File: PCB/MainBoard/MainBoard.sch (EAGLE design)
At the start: 79 parts, among them Q1 CSM-7X-DU, U1 STMICROELECTRONICS_STM32F446R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, U2 TI_NATIONAL_SEMICONDUCTOR_LM1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, U3 STMICROELECTRONICS_L78M05CDT-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

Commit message: Main board updates
-change mcu(STM32H753)
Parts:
- removed C20: 100nF, rcl:C-EUC0805
- removed C34: 10uF, rcl:C-EUC0805
- removed Q1: CSM-7X-DU, crystal:CSM-7X-DU
- removed U2: TI_NATIONAL_SEMICONDUCTOR_LM1117DT-3.3TI_NATIONAL_SEMICONDU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, TI National Semiconductor - LM1117DT-3.3:TI_NATIONAL_SEMICONDUCTOR_LM1117DT-3.3TI_NATIONAL_SEMICONDUCTOR_LM1117DT-3.3_0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
- removed U3: STMICROELECTRONICS_L78M05CDT-TRSTMICROELECTRONICS_L78M05CDT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, STMicroelectronics - L78M05CDT-TR:STMICROELECTRONICS_L78M05CDT-TRSTMICROELECTRONICS_L78M05CDT-TR_0_2
- added C40, C41, C42: 100nF, rcl:C-EUC0805
- added C43, C44, C45: 10uF, rcl:C-EUC0805
- added C46, C47: 22p, rcl:C-EUC0805
- added IC1: LD1085D2T33R, SamacSys_Parts:LD1085D2T33R
- added Q2: CSM-7X-DU, crystal:CSM-7X-DU
- added U4: STM32H753VIT6, STM32H753VIT6:STM32H753VIT6
- added U5: LM1084IS-5.0/NOPB, LM1084IS-5.0_NOPB:LM1084IS-5.0/NOPB
- C2, C3, C6, C7: device rcl:CPOL-EUC -> rcl:C-EUC0805
- C24: value 4,7uF(ceramic) -> 100nF
- C26: value 22p -> 2.2uf(ceramic)
- C27: value 22p -> 100uF
- U1: value STMICROELECTRONICS_STM32F446RET6STMICROELECTRONICS_STM32F446RET6_0_1 -> LM1084IS-5.0/NOPB; device STMicroelectronics - STM32F446RET6:STMICROELECTRONICS_STM32F446RET6STMICROELECTRONICS_STM32F446RET6_0_1 -> LM1084IS-5.0_NOPB:LM1084IS-5.0/NOPB
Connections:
- removed net BUTTON_1: U1B.PB15
- removed net BUTTON_2: U1B.PB14
- removed net BUTTON_3: U1B.PB13
- new net N$10: C47.1, Q2.2, U4G$1.PH0/OSC_IN
- new net N$11: C46.1, Q2.1, U4G$1.PH1/OSC_OUT
- new net N$12: U4G$2.PB10/QUADSPI_BK1_NCS
- new net N$13: U4G$2.PC9/QUADSPI_BK1_IO0
- new net N$14: U4G$2.PD11/QUADSPI_BK1_IO0
- new net N$15: U4G$2.PC10/QUADSPI_BK1_IO1
- new net N$16: U4G$2.PE2/QUADSPI_BK1_IO2
- new net N$19: U4G$2.PC11/QUADSPI_BK2_NCS
- new net N$20: U4G$2.PE7/QUADSPI_BK2_IO0
- new net N$22: U4G$2.PE9/QUADSPI_BK2_IO2
- new net N$23: U4G$2.PE10/QUADSPI_BK2_IO3
- new net N$25: U4G$2.PA5/SPI1_SCK/I2S1_CK
- new net N$26: U4G$2.PA6/SPI1_MISO/I2S1_SD
- new net N$27: U4G$2.PA7/SPI1_MOSI/I2S1_SDO
- new net N$28: U4G$2.PA15/SPI1_NSS/I2S1_WS
- new net N$29: U4G$2.PB3/SPI1_SCK/I2S1_CK
- new net N$30: U4G$2.PB4/SPI1_MISO/I2S1_SD
- new net N$31: U4G$2.PB5/SPI1_MOSI/I2S1_SDO
- new net N$32: U4G$2.PD7/SPI1_MOSI/I2S1_SDO
- new net N$33: U4G$3.PA0
- new net N$34: U4G$3.PA1
- new net N$35: U4G$3.PA2
- new net N$36: U4G$3.PA3
- new net N$37: U4G$3.PA8
- new net N$38: U4G$3.PB0
- new net N$39: U4G$3.PB1
- new net N$40: U4G$3.PB7
- new net N$41: U4G$3.PB8
- new net N$42: U4G$3.PB9
- new net N$43: U4G$3.PC0
- new net N$44: U4G$3.PC1
- new net N$47: U4G$3.PC4
- new net N$48: U4G$3.PC5
- new net N$49: U4G$3.PD0
- new net N$50: U4G$3.PD1
- new net N$51: U4G$3.PD2
- new net N$53: U4G$3.PD4
- new net N$54: U4G$3.PD5
- new net N$55: U4G$3.PE0
- new net N$56: U4G$3.PE1
- new net N$57: U4G$3.PE3
- new net N$58: U4G$3.PE4
- new net N$59: U4G$3.PE5
- new net N$60: U4G$3.PE6
- new net N$61: U4G$3.PE15
- new net N$62: U4G$3.PE14
- new net N$63: U4G$3.PE13
- new net N$64: U4G$3.PE12
- new net N$65: U4G$3.PE11
- new net N$66: U4G$3.PD15
- new net N$67: U4G$3.PD14
- new net N$68: U4G$3.PD10
- new net N$69: U4G$3.PD9
- new net N$70: U4G$3.PD8
- new net N$71: U4G$3.PD6
- new net N$72: U4G$3.PC13
- new net N$73: U4G$3.PC12
- new net N$74: U4G$3.PC8
- new net N$75: U4G$3.PC7
- new net N$76: U4G$3.PC6
- new net N$77: U4G$3.PB15
- new net N$78: U4G$3.PB14
- new net N$79: U4G$3.PB13
- new net N$80: U4G$3.PB12
- new net N$81: U4G$3.PB11
- new net N$82: U4G$3.PA12
- new net N$83: U4G$3.PA9
- new net N$84: U4G$3.PA10
- new net N$85: U4G$3.PA11
- new net N$86: U4G$1.PA13/JTMS-SWDIO
- new net N$87: U4G$1.PA14/JTCK-SWCLK
- net +3V3: now also C40.2, C41.2, C42.2, C43.2, C44.2, C45.2, U4G$1.VBAT, U4G$1.VDD, U4G$1.VDDA; no longer C20.2, C34.2, U1A.1_VDD, U1A.2_VDD, U1A.3_VDD, U1A.4_VDD, U1A.VBAT
- net +5V: now also C3.1, U1.OUTPUT; no longer C3.+, U3.OUT
- net 3V3: now also C7.1, IC1.OUTPUT; no longer C7.+, U2.OUT
- net A3V3: now also U4G$1.VREF+; no longer U1A.VDDA
- net BAT_ADC: no longer U1B.PA7
- net DIR_L1: no longer U1B.PC0
- net DIR_L2: no longer U1B.PC1
- net DIR_P1: no longer U1B.PC2
- net DIR_P2: no longer U1B.PC3
- net ENK_LP_A: no longer U1B.PA8
- net ENK_LP_B: no longer U1B.PA9
- net ENK_LT_A: no longer U1B.PA15
- net ENK_LT_B: no longer U1B.PB3
- net ENK_PP_A: no longer U1B.PC6
- net ENK_PP_B: no longer U1B.PC7
- net ENK_PT_A: no longer U1B.PB6
- net ENK_PT_B: no longer U1B.PB7
- net GND: now also C2.2, C24.2, C27.2, C3.2, C40.1, C41.1, C42.1, C43.1, C44.1, C45.1, C46.2, C47.2, C6.2, C7.2, IC1.GND, R1.1, U1.ADJ/GND, U4G$1.VSS, U4G$1.VSSA, U5.ADJ/GND; no longer C2.-, C20.1, C24.1, C27.1, C3.-, C34.1, C6.-, C7.-, R1.2, U1A.1_VSS, U1A.2_VSS, U1A.3_VSS, U1A.4_VSS, U1A.VSSA, U2.GND, U3.GND
- net KTIR_1: no longer U1B.PA4
- net KTIR_2: no longer U1B.PA5
- net KTIR_3: no longer U1B.PA6
- net LED_1: no longer U1B.PA12
- net LED_2: no longer U1B.PA11
- net LED_3: no longer U1B.PA10
- net N$1: now also C25.2, R2.1, U4G$1.!RST; no longer C26.2, Q1.1, U1B.PH1-OSC_OUT
- net N$17: now also U4G$2.PD12/QUADSPI_BK1_IO1; no longer U1B.PC8
- net N$18: now also U4G$2.PD13/QUADSPI_BK1_IO3; no longer U1B.PC9
- net N$2: now also U4G$2.PB2/QUADSPI_CLK; no longer C24.2, U1A.VCAP_1
- net N$21: now also U4G$2.PE8/QUADSPI_BK2_IO1; no longer U1B.PC12
- net N$24: now also U4G$2.PA4/SPI1_NSS/I2S1_WS; no longer U1B.PC15-OSC32_OUT
- net N$3: now also R1.2, U4G$1.BOOT0; no longer R1.1, U1B.BOOT0
- net N$4: now also C26.2, U4G$1.VCAP; no longer C27.2, Q1.2, U1B.PH0-OSC_IN
- net N$45: now also U4G$3.PC2_C; no longer U1B.PB4
- net N$46: now also U4G$3.PC3_C; no longer U1B.PB5
- net N$52: now also U4G$3.PD3; no longer U1B.PB12
- net N$8: now also U4G$2.PB6/QUADSPI_BK1_NCS; no longer U1B.PD2
- net NRST: no longer C25.2, R2.1, U1B.!RST!
- net PWM_LP: no longer U1B.PA0
- net PWM_LT: no longer U1B.PA1
- net PWM_PP: no longer U1B.PA2
- net PWM_PT: no longer U1B.PA3
- net RX: no longer U1B.PC11
- net SCL: no longer U1B.PB8
- net SDA: no longer U1B.PB9
- net SHARP_1: no longer U1B.PC4
- net SHARP_2: no longer U1B.PC5
- net SHARP_3: no longer U1B.PB0
- net SHARP_4: no longer U1B.PB1
- net SHARP_5: no longer U1B.PB2
- net SHARP_6: no longer U1B.PB10
- net SWCLK: no longer U1B.PA14
- net SWDIO: no longer U1B.PA13
- net S_KILL: no longer U1B.PC14-OSC32_IN
- net S_START: no longer U1B.PC13
- net TX: no longer U1B.PC10
- net V_BAT: now also C2.1, C24.1, C27.1, C6.1, IC1.INPUT, U1.INPUT, U5.INPUT, U5.OUTPUT; no longer C2.+, C6.+, U2.IN, U3.IN
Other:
- moved on the sheet: C24, C25, C26, C27, C38, C39, C4, C5, C8, R1, R2, R9

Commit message: Update eagle files
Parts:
- removed C1, C4: 100nF, rcl:C-EUC0805
- removed C2, C3: 100uF, rcl:C-EUC0805
- removed U1: LM1084IS-5.0/NOPB, LM1084IS-5.0_NOPB:LM1084IS-5.0/NOPB
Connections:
- new net N$88: C24.2, C27.2, U5.ADJ/GND
- net +5V: now also C5.1, C6.1, IC1.INPUT, U5.OUTPUT; no longer C3.1, C4.1, U1.OUTPUT
- net GND: no longer C1.2, C2.2, C24.2, C27.2, C3.2, C4.2, U1.ADJ/GND, U5.ADJ/GND
- net V_BAT: no longer C1.1, C2.1, C5.1, C6.1, IC1.INPUT, U1.INPUT, U5.OUTPUT
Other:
- moved on the sheet: C24, C27, C5, C6, U5

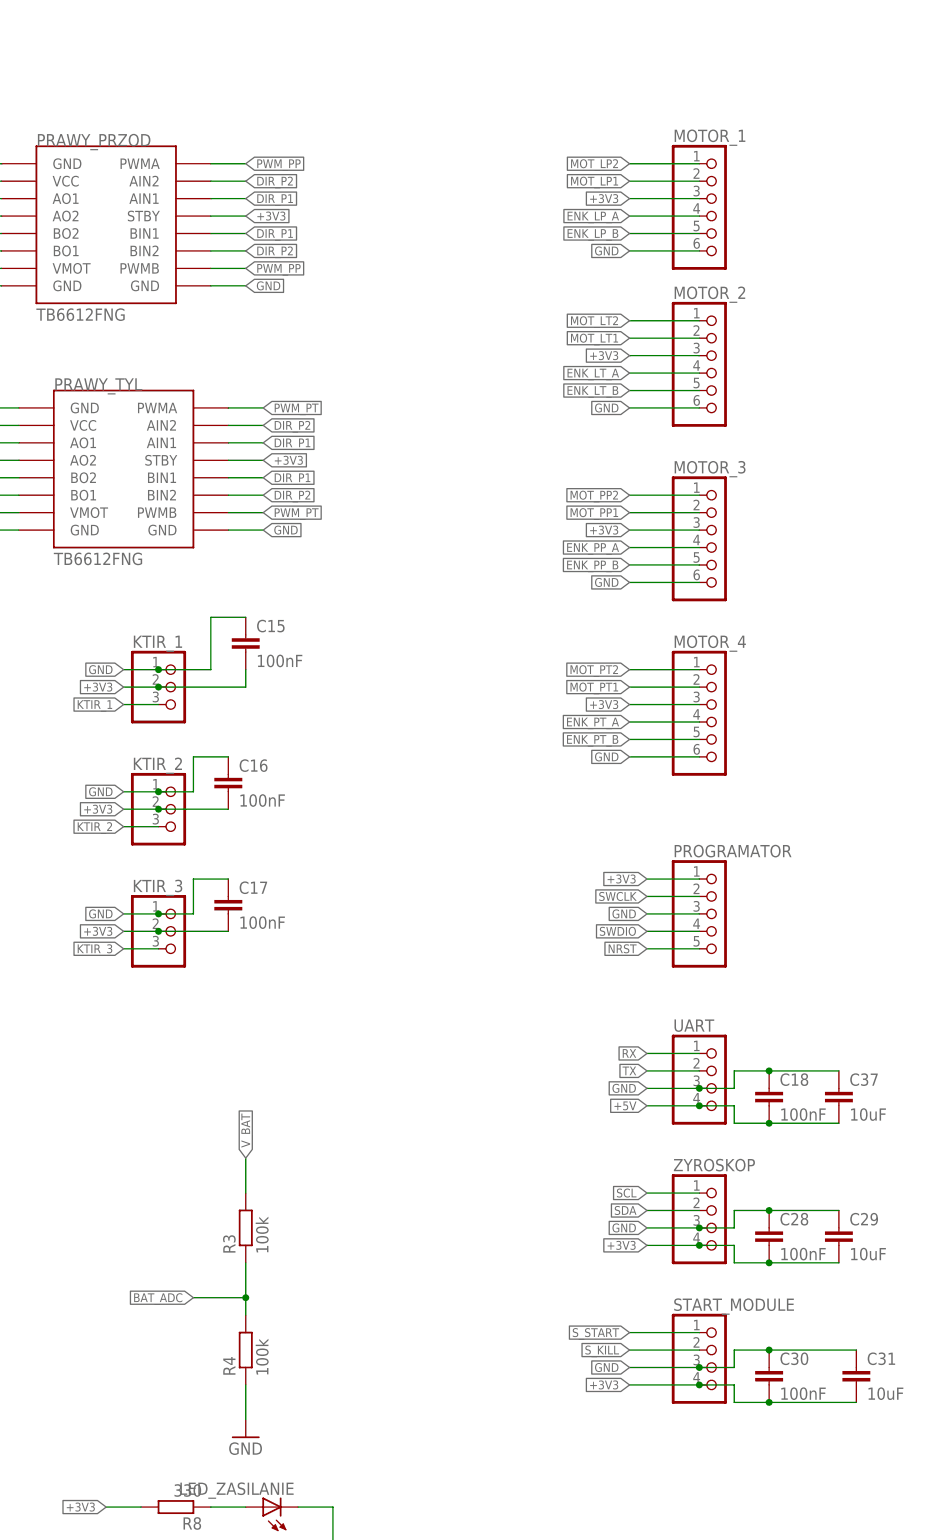
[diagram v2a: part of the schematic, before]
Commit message: PCB update
-place elements on the board
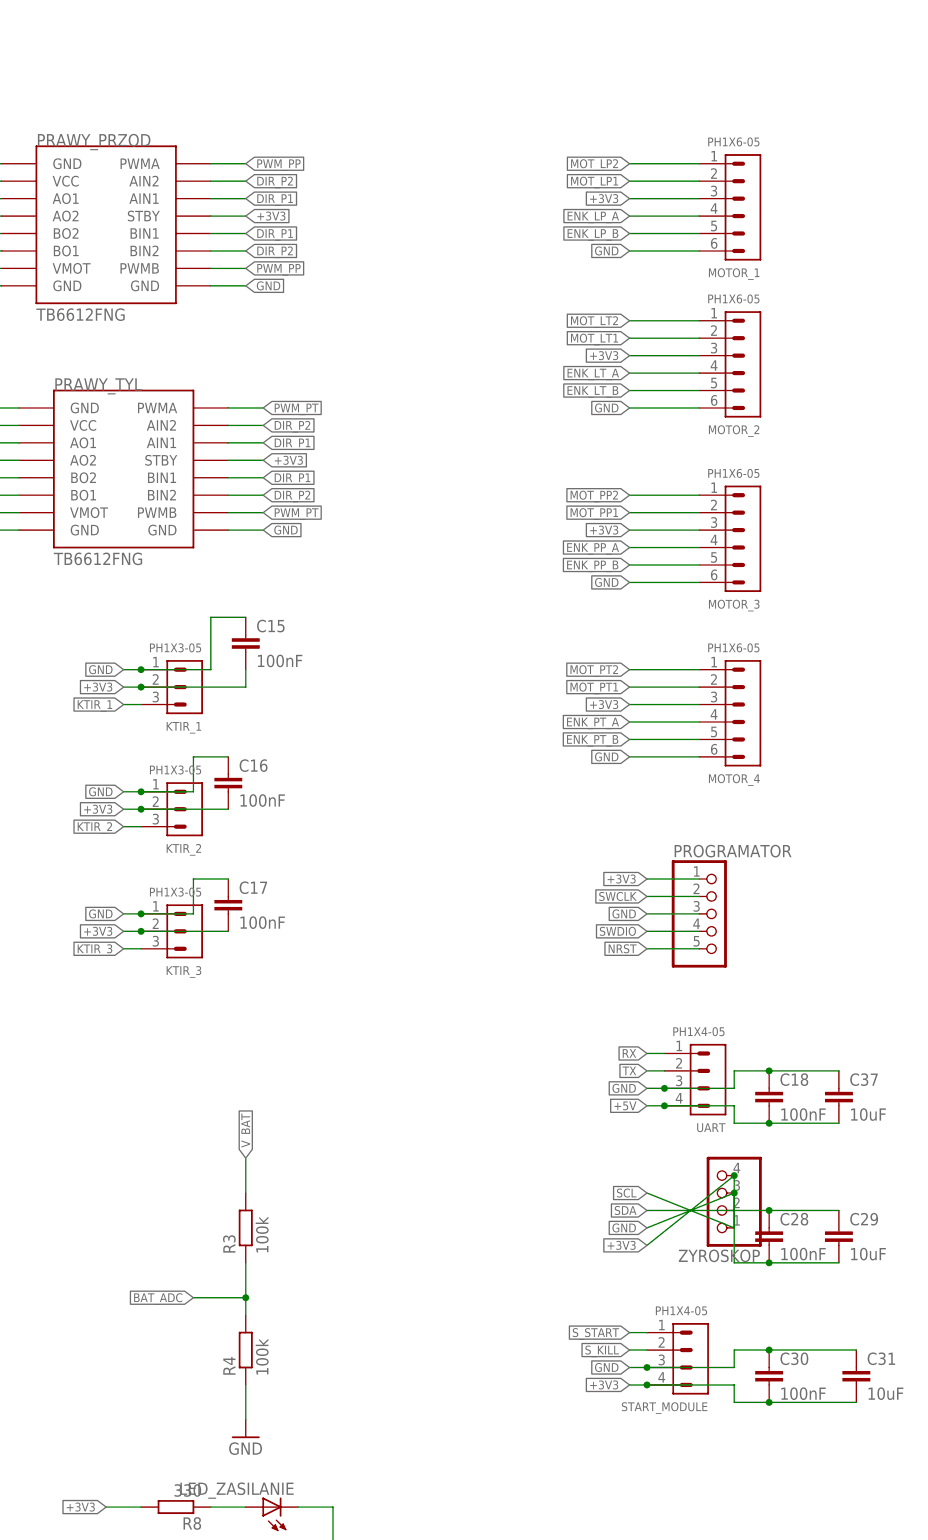
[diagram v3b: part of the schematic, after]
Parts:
- KTIR_1, KTIR_2, KTIR_3: value (none) -> PH1X3-05; device pinhead:PINHD-1X3 -> pinhrad:PH1X3-05
- MOTOR_1, MOTOR_2, MOTOR_3, MOTOR_4: value (none) -> PH1X6-05; device pinhead:PINHD-1X6 -> pinhrad:PH1X6-05
- START_MODULE, UART: value (none) -> PH1X4-05; device pinhead:PINHD-1X4 -> pinhrad:PH1X4-05
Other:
- moved on the sheet: ZYROSKOP

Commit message: Update pcb files
- edit positions on the board
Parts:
- added R13: 100R, rcl:R-EU_M0805
- added R14, R15: 47R, rcl:R-EU_M0805
- PROGRAMATOR: value (none) -> FTSH-107-01-F-DV-K; device pinhead:PINHD-1X5 -> FTSH-107-01-F-DV-K:FTSH-107-01-F-DV-K
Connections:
- net N$30 renamed JRST
- removed net N$18: U4G$2.PD13/QUADSPI_BK1_IO3
- removed net N$22: U4G$2.PE9/QUADSPI_BK2_IO2
- removed net N$24: U4G$2.PA4/SPI1_NSS/I2S1_WS
- removed net N$25: U4G$2.PA5/SPI1_SCK/I2S1_CK
- removed net N$26: U4G$2.PA6/SPI1_MISO/I2S1_SD
- removed net N$27: U4G$2.PA7/SPI1_MOSI/I2S1_SDO
- removed net N$28: U4G$2.PA15/SPI1_NSS/I2S1_WS
- removed net N$29: U4G$2.PB3/SPI1_SCK/I2S1_CK
- removed net N$31: U4G$2.PB5/SPI1_MOSI/I2S1_SDO
- removed net N$33: U4G$3.PA0
- removed net N$34: U4G$3.PA1
- removed net N$38: U4G$3.PB0
- removed net N$40: U4G$3.PB7
- removed net N$43: U4G$3.PC0
- removed net N$63: U4G$3.PE13
- removed net N$65: U4G$3.PE11
- removed net N$67: U4G$3.PD14
- removed net N$74: U4G$3.PC8
- removed net N$75: U4G$3.PC7
- removed net N$76: U4G$3.PC6
- removed net N$86: U4G$1.PA13/JTMS-SWDIO
- removed net N$87: U4G$1.PA14/JTCK-SWCLK
- removed net SWCLK: PROGRAMATOR.2
- removed net SWDIO: PROGRAMATOR.4
- new net JCLK: R15.1, U4G$1.PA14/JTCK-SWCLK
- new net JTDI: PROGRAMATOR.10, U4G$2.PA15/SPI1_NSS/I2S1_WS
- new net JTDO: PROGRAMATOR.08, U4G$2.PB3/SPI1_SCK/I2S1_CK
- new net JTMS: PROGRAMATOR.04, U4G$1.PA13/JTMS-SWDIO
- net +3V3: now also PROGRAMATOR.03; no longer PROGRAMATOR.1
- net BAT_ADC: now also U4G$3.PC0
- net ENK_LP_A: now also U4G$2.PE9/QUADSPI_BK2_IO2
- net ENK_LP_B: now also U4G$3.PE11
- net ENK_LT_B: now also U4G$2.PA7/SPI1_MOSI/I2S1_SDO, U4G$2.PB5/SPI1_MOSI/I2S1_SDO
- net ENK_PP_A: now also U4G$2.PD12/QUADSPI_BK1_IO1
- net ENK_PP_B: now also U4G$2.PD13/QUADSPI_BK1_IO3
- net ENK_PT_A: now also U4G$3.PC6
- net ENK_PT_B: now also U4G$3.PC7
- net GND: now also PROGRAMATOR.05, PROGRAMATOR.07, R13.2; no longer PROGRAMATOR.3
- net KTIR_1: now also U4G$2.PA4/SPI1_NSS/I2S1_WS
- net KTIR_2: now also U4G$2.PA5/SPI1_SCK/I2S1_CK
- net KTIR_3: now also U4G$2.PA6/SPI1_MISO/I2S1_SD
- net N$1: now also PROGRAMATOR.11, R13.1; no longer C25.2, R2.1, U4G$1.!RST
- net N$17: now also PROGRAMATOR.06, R15.2; no longer U4G$2.PD12/QUADSPI_BK1_IO1
- net N$8: now also PROGRAMATOR.12, R14.2; no longer U4G$2.PB6/QUADSPI_BK1_NCS
- net NRST: now also C25.2, R14.1, R2.1, U4G$1.!RST; no longer PROGRAMATOR.5
- net PWM_LP: now also U4G$3.PE13
- net PWM_LT: now also U4G$3.PB0
- net PWM_PP: now also U4G$3.PD14
- net PWM_PT: now also U4G$3.PC8
- net RX: now also U4G$3.PA0
- net SCL: now also U4G$2.PB6/QUADSPI_BK1_NCS
- net SDA: now also U4G$3.PB7
- net TX: now also U4G$3.PA1
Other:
- moved on the sheet: ZYROSKOP

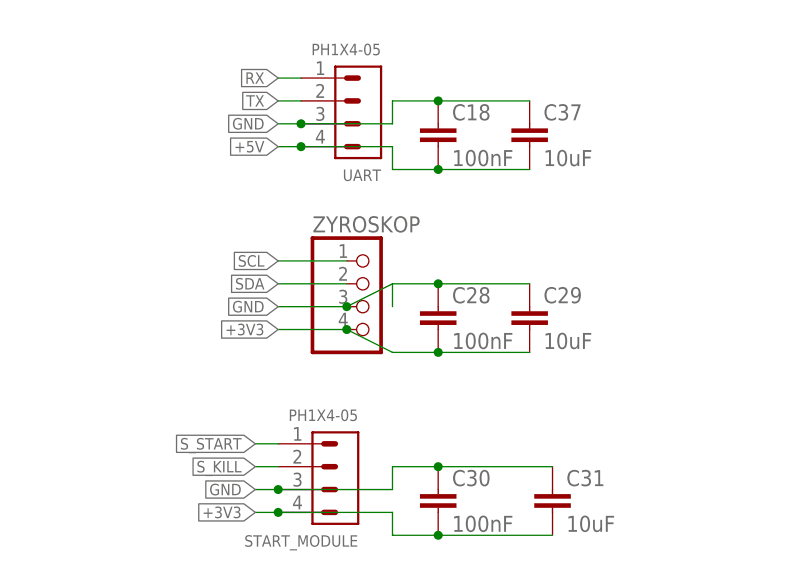
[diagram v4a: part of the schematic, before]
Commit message: Update eagle files
-delete gyroscope
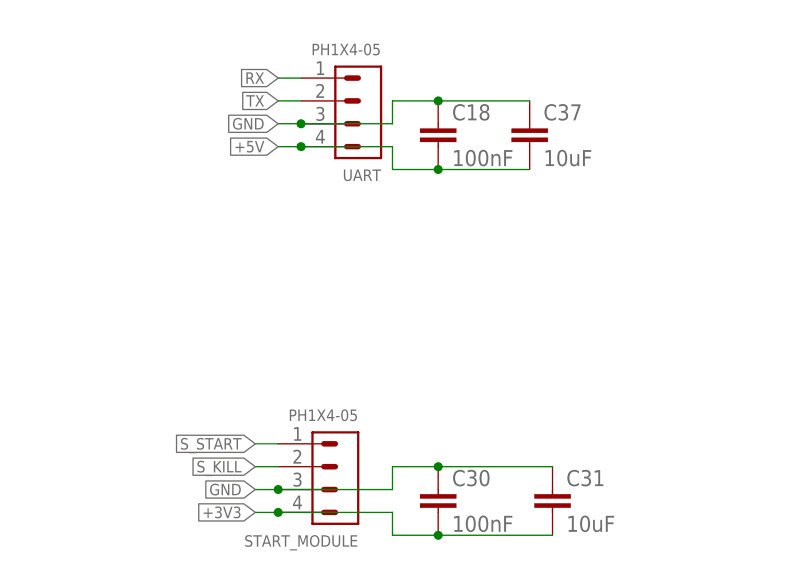
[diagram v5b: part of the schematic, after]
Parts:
- removed C28: 100nF, rcl:C-EUC0805
- removed C29: 10uF, rcl:C-EUC0805
- removed ZYROSKOP: (no value), pinhead:PINHD-1X4
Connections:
- net +3V3: no longer C28.2, C29.2, ZYROSKOP.4
- net GND: no longer C28.1, C29.1, ZYROSKOP.3
- net SCL: no longer ZYROSKOP.1
- net SDA: no longer ZYROSKOP.2
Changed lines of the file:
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@@
 <part name="GND8" library="supply1" deviceset="GND" device=""/>
 <part name="UART" library="pinhrad" deviceset="PH1X4" device="-05"/>
-<part name="ZYROSKOP" library="pinhead" deviceset="PINHD-1X4" device=""/>
 <part name="LED1" library="led" deviceset="LED" device="CHIPLED_0805"/>
 <part name="LED2" library="led" deviceset="LED" device="CHIPLED_0805"/>
@@
 <part name="R8" library="rcl" deviceset="R-EU_" device="M0805" value="330"/>
 <part name="LED_ZASILANIE" library="led" deviceset="LED" device="CHIPLED_0805"/>
-<part name="C28" library="rcl" deviceset="C-EU" device="C0805" value="100nF"/>
-<part name="C29" library="rcl" deviceset="C-EU" device="C0805" value="10uF"/>
 <part name="C30" library="rcl" deviceset="C-EU" device="C0805" value="100nF"/>
 <part name="C31" library="rcl" deviceset="C-EU" device="C0805" value="10uF"/>
@@
 <instance part="GND8" gate="1" x="205.74" y="-106.68"/>
 <instance part="UART" gate="G$1" x="274.32" y="-50.8" rot="R180"/>
-<instance part="ZYROSKOP" gate="A" x="274.32" y="-76.2"/>
 <instance part="LED1" gate="G$1" x="205.74" y="-127" rot="R90"/>
 <instance part="LED2" gate="G$1" x="205.74" y="-137.16" rot="R90"/>
@@
 <instance part="R8" gate="G$1" x="195.58" y="-116.84" rot="R180"/>
 <instance part="LED_ZASILANIE" gate="G$1" x="208.28" y="-116.84" rot="R90"/>
-<instance part="C28" gate="G$1" x="281.94" y="-76.2"/>
-<instance part="C29" gate="G$1" x="292.1" y="-76.2"/>
 <instance part="C30" gate="G$1" x="281.94" y="-96.52"/>
 <instance part="C31" gate="G$1" x="294.64" y="-96.52"/>
@@
 </segment>
 <segment>
-<pinref part="ZYROSKOP" gate="A" pin="3"/>
-<wire x1="271.78" y1="-76.2" x2="264.16" y2="-76.2" width="0.1524" layer="91"/>
-<label x="264.16" y="-76.2" size="1.27" layer="95" rot="R180" xref="yes"/>
-<pinref part="C29" gate="G$1" pin="1"/>
-<pinref part="C28" gate="G$1" pin="1"/>
-<wire x1="292.1" y1="-73.66" x2="281.94" y2="-73.66" width="0.1524" layer="91"/>
-<wire x1="281.94" y1="-73.66" x2="276.86" y2="-73.66" width="0.1524" layer="91"/>
-<wire x1="276.86" y1="-73.66" x2="276.86" y2="-76.2" width="0.1524" layer="91"/>
-<junction x="281.94" y="-73.66"/>
-<wire x1="276.86" y1="-73.66" x2="271.78" y2="-76.2" width="0.1524" layer="91"/>
-<junction x="271.78" y="-76.2"/>
-</segment>
-<segment>
 <pinref part="LED1" gate="G$1" pin="C"/>
 <pinref part="GND9" gate="1" pin="GND"/>
@@
 </segment>
 <segment>
-<pinref part="ZYROSKOP" gate="A" pin="4"/>
-<wire x1="271.78" y1="-78.74" x2="264.16" y2="-78.74" width="0.1524" layer="91"/>
-<label x="264.16" y="-78.74" size="1.27" layer="95" rot="R180" xref="yes"/>
-<wire x1="271.78" y1="-78.74" x2="276.86" y2="-81.28" width="0.1524" layer="91"/>
-<junction x="271.78" y="-78.74"/>
-<pinref part="C28" gate="G$1" pin="2"/>
-<wire x1="276.86" y1="-81.28" x2="281.94" y2="-81.28" width="0.1524" layer="91"/>
-<pinref part="C29" gate="G$1" pin="2"/>
-<wire x1="281.94" y1="-81.28" x2="292.1" y2="-81.28" width="0.1524" layer="91"/>
-<junction x="281.94" y="-81.28"/>
-</segment>
-<segment>
 <pinref part="START_MODULE" gate="G$1" pin="4"/>
 <wire x1="264.16" y1="-99.06" x2="261.62" y2="-99.06" width="0.1524" layer="91"/>
@@
 <net name="SCL" class="0">
 <segment>
-<pinref part="ZYROSKOP" gate="A" pin="1"/>
-<wire x1="271.78" y1="-71.12" x2="264.16" y2="-71.12" width="0.1524" layer="91"/>
-<label x="264.16" y="-71.12" size="1.27" layer="95" rot="R180" xref="yes"/>
-</segment>
-<segment>
 <pinref part="U4" gate="G$2" pin="PB6/QUADSPI_BK1_NCS"/>
 <wire x1="-243.84" y1="66.04" x2="-248.92" y2="66.04" width="0.1524" layer="91"/>
@@
 <net name="SDA" class="0">
 <segment>
-<pinref part="ZYROSKOP" gate="A" pin="2"/>
-<wire x1="271.78" y1="-73.66" x2="264.16" y2="-73.66" width="0.1524" layer="91"/>
-<label x="264.16" y="-73.66" size="1.27" layer="95" rot="R180" xref="yes"/>
-</segment>
-<segment>
 <pinref part="U4" gate="G$3" pin="PB7"/>
